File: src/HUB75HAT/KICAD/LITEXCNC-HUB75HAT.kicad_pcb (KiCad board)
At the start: 2 copper layers, 143.5 x 91.4 mm, 114 parts, among them J10 Conn_01x02, J11 HUB75, J12 HUB75, J13 V7.0, J14 V8.0, J15 HUB75, J16 HUB75, J17 Conn_02x20_Odd_Even, J4 HUB75, J5 HUB75, J6 HUB75, J7 v7.0, J8 v8.0, J9 HUB75, U1 74CB3T3245, U10 MAX3485, U11 74HC04, U12 MAX3485, U2 74CB3T3245, U3 74CB3T3245, U4 74CB3T3245, U5 74CB3T3245, U6 74CB3T3245, U7 74HC04, U8 74CB3T3245, U9 74HC04

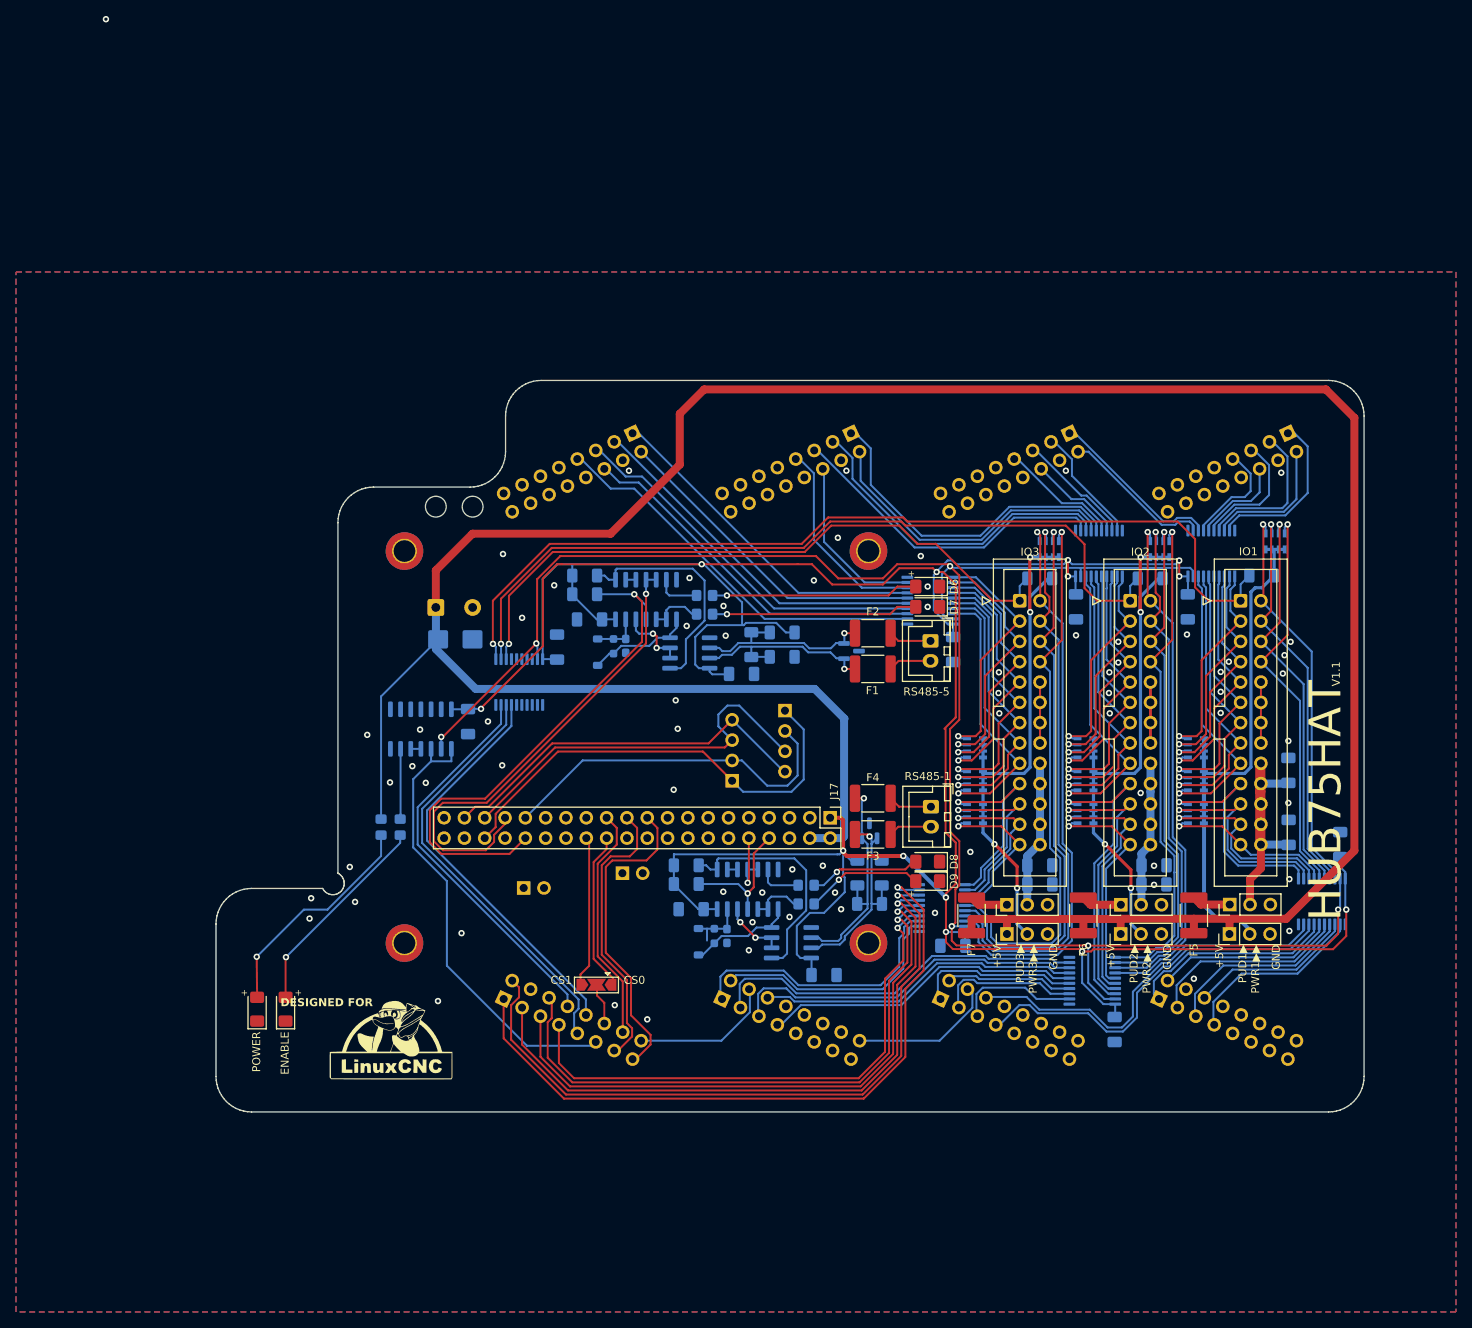
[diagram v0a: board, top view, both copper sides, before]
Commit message: Solved problem with J17 (GPIO header)
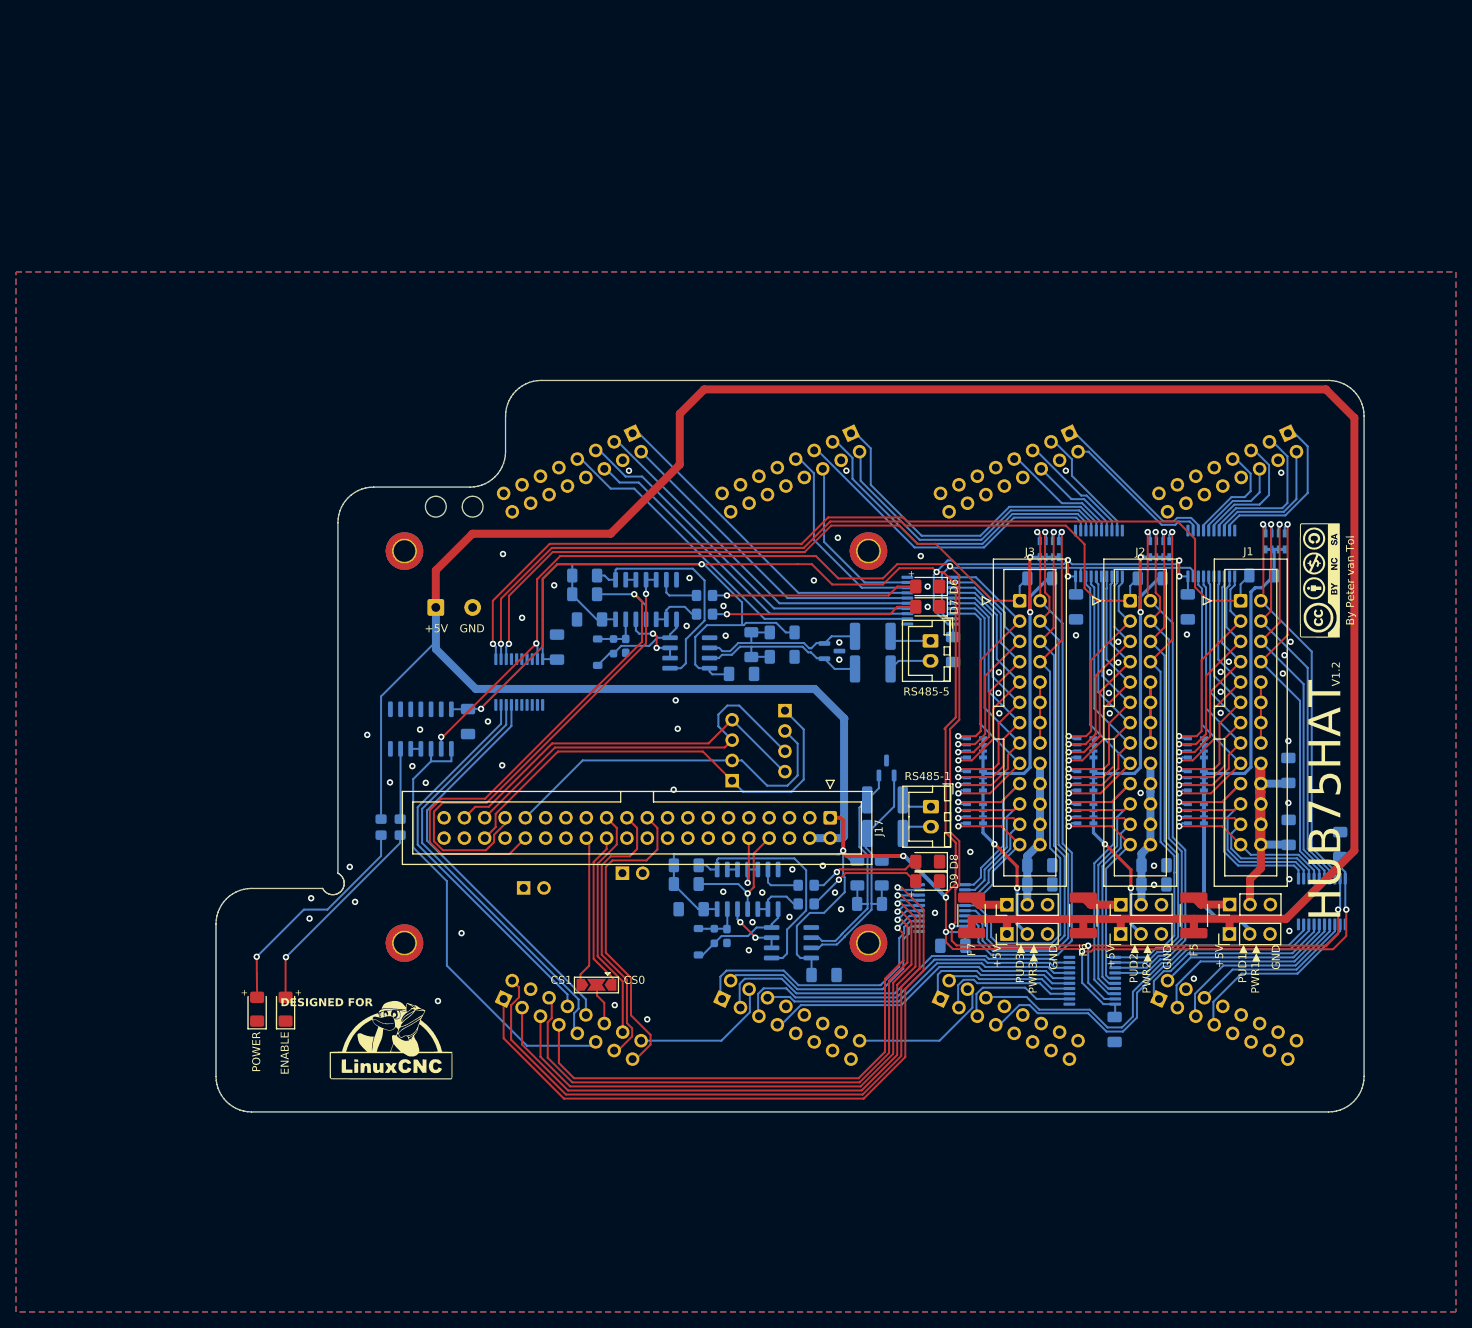
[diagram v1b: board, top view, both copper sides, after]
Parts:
- removed D12: SM6T6V8A, Diode_SMD:D_SMB
- added G***: LOGO, LOGO, F.Cu at (274.1, -100.3)
- F1, F2, F3, F4: moved to B.Cu
- J17: footprint Connector_PinHeader_2.54mm:PinHeader_2x20_P2.54mm_Vertical -> Connector_IDC:IDC-Header_2x20_P2.54mm_Vertical
- moved D11 8.13 mm to (219.9, -76.9)
- moved D5 2.45 mm to (213.1, -91.5)
- moved F4 1.54 mm to (219.7, -72.9)
- moved F3 1.53 mm to (219.7, -68.7)
- moved F2 0.39 mm to (218.2, -93.3)
- renumbered IO1 to J1, IO2 to J2, IO3 to J3
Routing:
- net Net-(D11-A1): track 25.9 -> 31.7 mm, vias 1 -> 0
- net Net-(D11-A2): track 28.2 -> 30.6 mm, vias 1 -> 0
- net Net-(J21-Pin_1): track 5.48 -> 3.87 mm
- net Net-(J21-Pin_2): track 5.44 -> 3.86 mm
- net Net-(D10-A): track 7.54 -> 6.07 mm
- net Net-(D5-A1): track 24.8 -> 23.6 mm, vias 1 -> 0
- net Net-(D5-A2): track 24.2 -> 23.3 mm, vias 1 -> 0
- net Net-(J20-Pin_1): track 5.39 -> 6.04 mm
- net GND: vias 70 -> 72
- net (no net): vias 1 -> 0
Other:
- board text added: "By Peter van Tol"
- board text added: "V1.2"
- board text removed: "V1.1"
